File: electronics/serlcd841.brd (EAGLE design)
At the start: 42.4 x 15 mm, 12 parts, among them IC1 T841, J1 AVRISP, Q1 3904

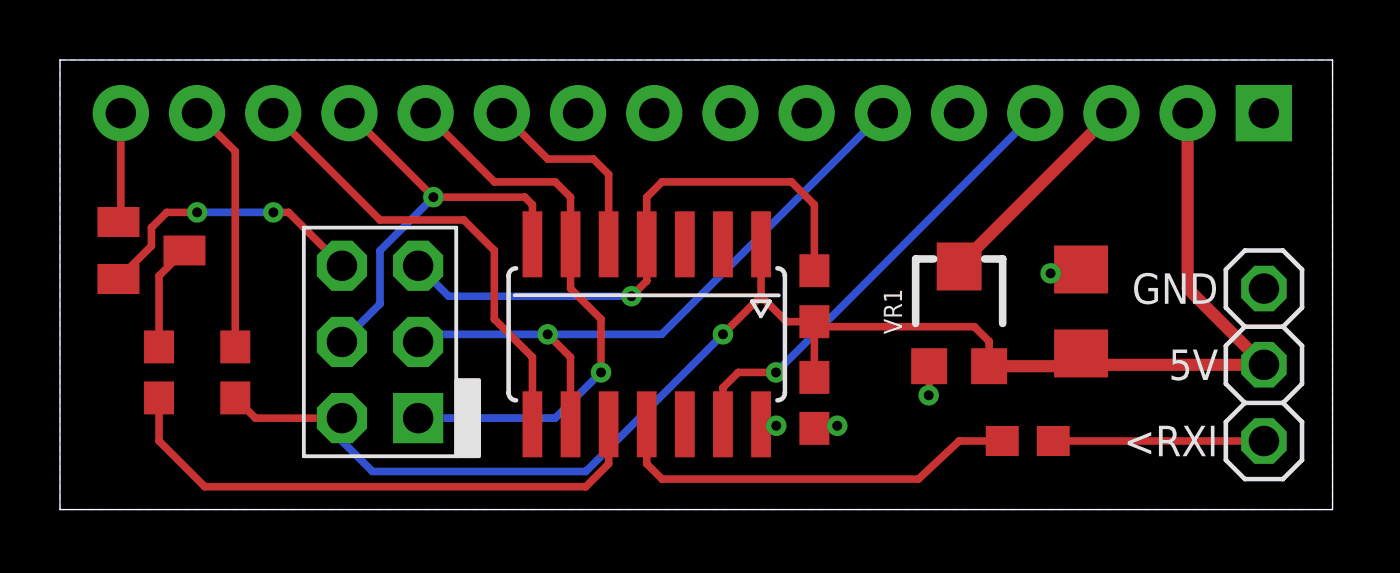
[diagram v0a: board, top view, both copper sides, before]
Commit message: updated footprint for lcd, layout tweaks, switched some pins.
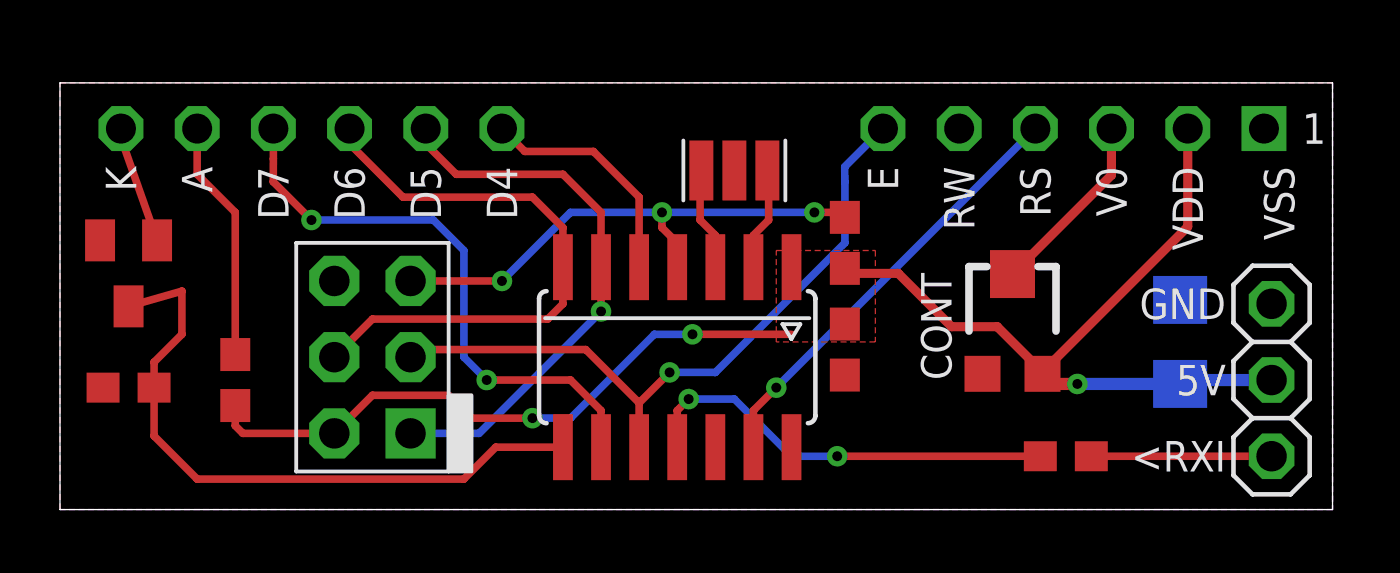
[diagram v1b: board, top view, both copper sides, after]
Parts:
- removed LCD1: LCD-16X2NOHOLES, SparkFun-Displays:LCD-16X2_NOHOLESNOSILK
- removed R4: 10K, bt_rcl:0603
- added LCD2: LCD-44780-4BIT, bt_display:LCD16SIP
- added Q2: 16MHz, bt_crystal:CSTCE_V_C
- added R1: 10K, bt_rcl:0603
- Q1: value 3904 -> 7000
- R3: value 330 -> 220
- moved C2 3.45 mm to (37.3, 5.59), flipped to the bottom
- moved R2 2.05 mm to (26.2, 8.89)
- moved C1 2.05 mm to (26.2, 5.33)
- moved VR1 1.80 mm to (31.8, 6.35)
- moved R5 1.37 mm to (33.5, 1.78)
- moved IC1 1.27 mm to (20.6, 5.08)
- moved Q1 1.08 mm to (2.29, 7.87), turned to 180 degrees
- moved JP1 0.57 mm to (40.4, 4.32)
- moved J1 0.57 mm to (10.4, 5.08)
- moved R3 0.25 mm to (5.84, 4.32)
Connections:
- removed net DB4: IC1.5, LCD1.11
- removed net DB5: IC1.6, J1.1, LCD1.12
- removed net DB6: IC1.7, J1.4, LCD1.13
- removed net DB7: IC1.8, LCD1.14
- removed net E: IC1.9, J1.3, LCD1.6
- removed net N$1: Q1.3, R4.1
- new net N$2: IC1.2, Q2.X2
- new net N$3: IC1.3, Q2.X1
- new net PA3: IC1.10, J1.3, LCD2.E
- new net PA4: IC1.9, LCD2.D7
- new net PA6: IC1.7, J1.4, LCD2.D6
- new net PA7: IC1.6, J1.1, LCD2.D5
- new net PB2: IC1.5, LCD2.D4
- net A: now also LCD2.A; no longer LCD1.15
- net GND: now also LCD2.RW, LCD2.VSS, Q2.GND, R1.1; no longer LCD1.1, LCD1.5
- net K: now also LCD2.K; no longer LCD1.16
- net LIGHT: now also IC1.8, Q1.3, R1.2; no longer IC1.10, R4.2
- net RS: now also LCD2.RS; no longer LCD1.4
- net VCC: now also LCD2.VDD; no longer LCD1.2
- net VO: now also LCD2.V0; no longer LCD1.3
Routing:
- net PA3: track 0.00 -> 23.3 mm, vias 0 -> 1
- net E: track 22.0 -> 0.00 mm, vias 1 -> 0
- net PA6: track 0.00 -> 19.7 mm
- net PA4: track 0.00 -> 19.2 mm, vias 0 -> 2
- net DB5: track 19.0 -> 0.00 mm, vias 1 -> 0
- net PA7: track 0.00 -> 18.6 mm, vias 0 -> 1
- net DB7: track 15.6 -> 0.00 mm
- net DB6: track 14.8 -> 0.00 mm, vias 1 -> 0
- net GND: track 12.7 -> 0.18 mm, vias 6 -> 0
- net PB2: track 0.00 -> 7.86 mm
- net DB4: track 6.74 -> 0.00 mm
- net VCC: track 53.0 -> 47.6 mm, vias 1 -> 3
- net N$1: track 3.56 -> 0.00 mm
- net N$3: track 0.00 -> 3.43 mm
- net N$2: track 0.00 -> 3.43 mm
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- added copper zone on layer 1, net GND
- added copper zone on layer 1, net VCC
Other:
- board size 42.4 x 15 mm -> 42.4 x 14.2 mm
- board text added: "CONT"

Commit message: backlight nmos rotation
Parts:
- moved Q1 0.57 mm to (2.79, 8.13), turned to 270 degrees
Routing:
- net LIGHT: track 21.7 -> 20.8 mm
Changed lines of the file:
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@@
 <attribute name="VALUE" x="43.561" y="0.508" size="1.27" layer="27" rot="R90"/>
 </element>
-<element name="Q1" library="bt_transistor" package="SOT-23" value="7000" x="2.286" y="7.874" smashed="yes" rot="R180">
-<attribute name="VALUE" x="3.175" y="6.35" size="0.8128" layer="27" font="vector" ratio="10" rot="R270" align="bottom-center"/>
+<element name="Q1" library="bt_transistor" package="SOT-23" value="7000" x="2.794" y="8.128" smashed="yes" rot="R270">
+<attribute name="VALUE" x="2.54" y="6.223" size="0.8128" layer="27" font="vector" ratio="10" rot="R180" align="bottom-center"/>
 </element>
 <element name="R2" library="bt_rcl" package="0603" value="10K" x="26.162" y="8.89" smashed="yes" rot="R270">
@@
 <signal name="K">
 <contactref element="Q1" pad="1"/>
-<wire x1="3.236" y1="8.974" x2="1.948" y2="12.626" width="0.254" layer="1"/>
+<wire x1="1.694" y1="9.078" x2="1.694" y2="12.372" width="0.254" layer="1"/>
 <contactref element="LCD2" pad="K"/>
 <wire x1="2.032" y1="12.7" x2="2.022" y2="12.7" width="0.254" layer="1"/>
-<wire x1="2.022" y1="12.7" x2="1.948" y2="12.626" width="0.254" layer="1"/>
+<wire x1="2.022" y1="12.7" x2="1.694" y2="12.372" width="0.254" layer="1"/>
 </signal>
 <signal name="PB2">
@@
 <wire x1="3.136" y1="4.064" x2="3.136" y2="4.914" width="0.254" layer="1"/>
 <wire x1="3.136" y1="4.914" x2="4.064" y2="5.842" width="0.254" layer="1"/>
-<wire x1="4.064" y1="5.842" x2="4.064" y2="7.282" width="0.254" layer="1"/>
-<wire x1="4.064" y1="7.282" x2="2.286" y2="6.774" width="0.254" layer="1"/>
+<wire x1="4.064" y1="5.842" x2="4.064" y2="8.044" width="0.254" layer="1"/>
+<wire x1="4.064" y1="8.044" x2="3.894" y2="8.128" width="0.254" layer="1"/>
 <wire x1="3.136" y1="4.064" x2="3.136" y2="2.452" width="0.254" layer="1"/>
 <wire x1="3.136" y1="2.452" x2="4.572" y2="1.016" width="0.254" layer="1"/>

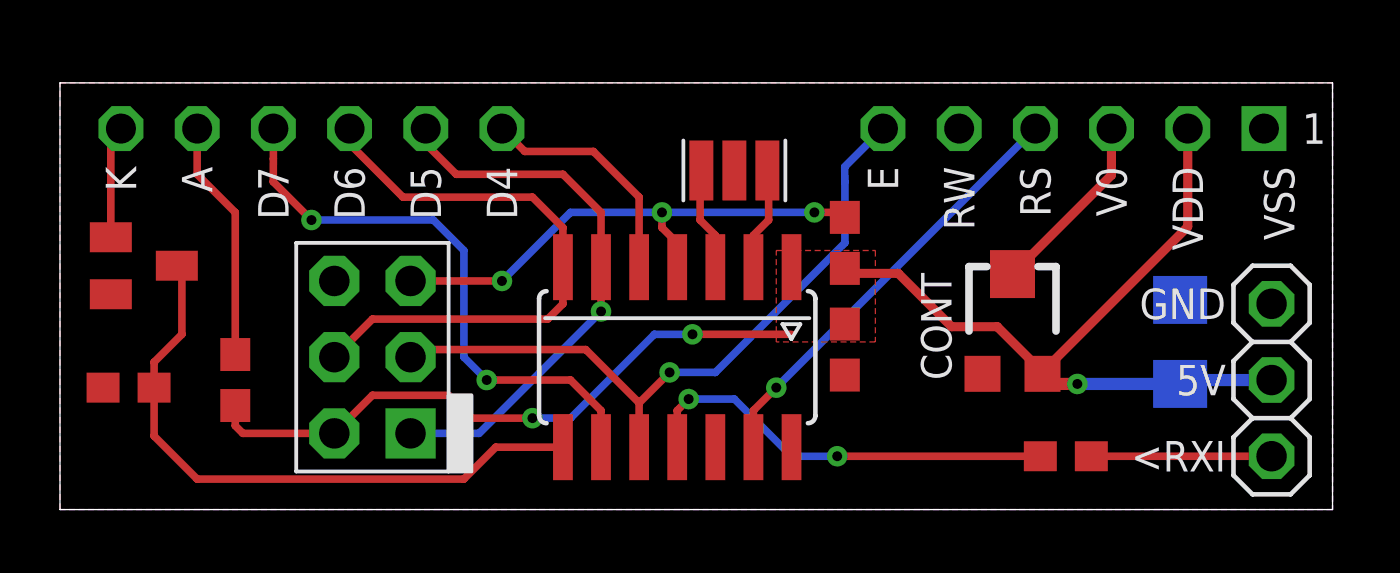
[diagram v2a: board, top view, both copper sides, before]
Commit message: Corrected ISP connections, removed transistor for
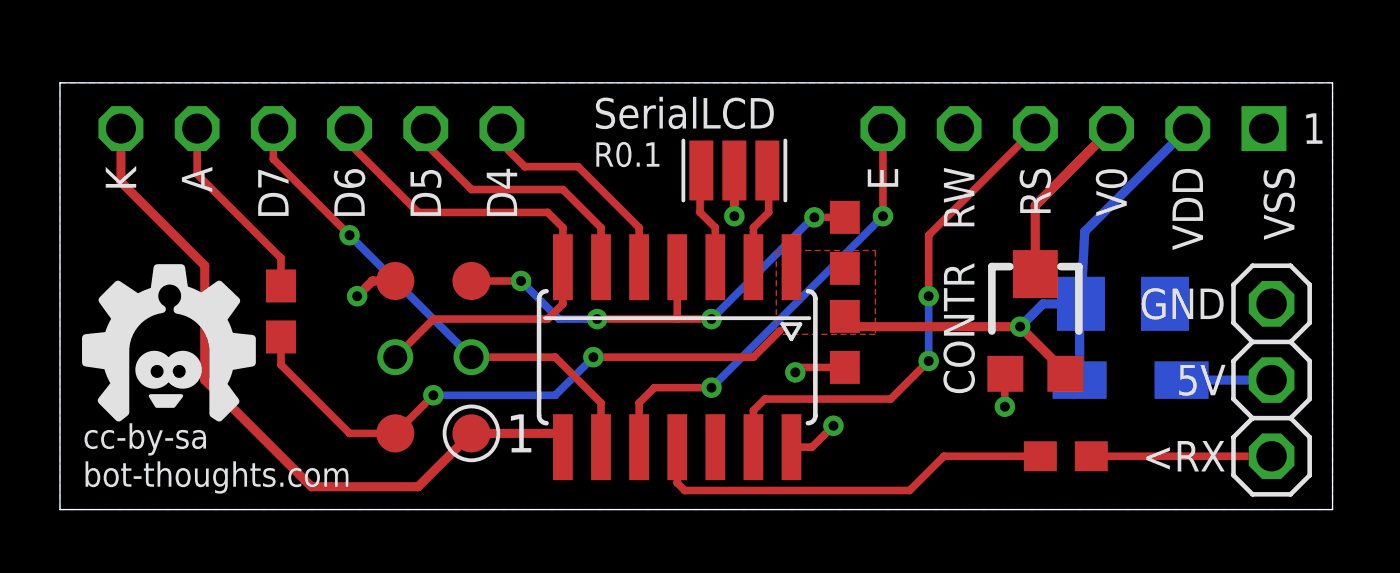
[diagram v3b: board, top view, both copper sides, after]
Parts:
- removed Q1: 7000, bt_transistor:SOT-23
- removed R1: 10K, bt_rcl:0603
- added D1: MBR1020VL, bt_diode:SOD123FL
- added U$6: BTLOGO-LOGO-MD, bt:BTLOGOM
- J1: device bt_avr:CON6P2R -> bt_avr:2X3_TP
- moved R3 2.75 mm to (7.37, 6.60)
- moved C2 2.29 mm to (35.4, 6.86), turned to 180 degrees
- moved J1 2.03 mm to (12.4, 5.08), turned to 180 degrees
- moved VR1 0.76 mm to (32.5, 6.35)
- moved C1 0.25 mm to (26.2, 5.59)
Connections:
- removed net K: LCD2.K, Q1.1
- removed net LIGHT: IC1.8, Q1.3, R1.2
- new net N$1: D1.A, JP1.2
- new net PA5: IC1.8, J1.1, LCD2.K
- net GND: no longer Q1.2, R1.1
- net PA3: no longer J1.3
- net PA4: now also J1.3
- net PA7: no longer J1.1
- net VCC: now also D1.C; no longer JP1.2
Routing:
- net PA5: track 0.00 -> 24.1 mm
- net LIGHT: track 20.8 -> 0.00 mm
- net PA7: track 18.6 -> 8.83 mm, vias 1 -> 0
- net PA3: track 23.3 -> 15.1 mm, vias 1 -> 2
- net GND: track 0.18 -> 7.70 mm, vias 0 -> 5
- net VCC: track 47.6 -> 40.4 mm
- net K: track 3.77 -> 0.00 mm
- net VO: track 6.22 -> 9.51 mm
- net N$1: track 0.00 -> 3.00 mm
- net RS: track 14.5 -> 17.0 mm, vias 1 -> 2
- net PA4: track 19.2 -> 16.8 mm, vias 2 -> 1
- net PA6: track 19.7 -> 17.6 mm
- net A: track 8.06 -> 6.41 mm
- net RESET: track 17.6 -> 16.4 mm, vias 3 -> 4
- net RX: track 14.3 -> 13.9 mm, vias 2 -> 0
- removed copper zone on layer 1, net GND
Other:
- board text added: "<RX"
- board text added: "CONTR"
- board text added: "R0.1"
- board text added: "SerialLCD"
- board text added: "bot-thoughts.com"
- board text added: "cc-by-sa"
- board text removed: "<RXI"
- board text removed: "CONT"
